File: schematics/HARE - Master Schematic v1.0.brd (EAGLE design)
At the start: 105.1 x 80 mm, 106 parts, among them IC1 NE5532N, IC2 NE5532N, IC3 FT232RL, IC4 NE5532N, IC5 7805DT, IC6 AT25P, J1 9V, J2 STEREOSW, J3 STEREOSW, Q1 16 MHz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

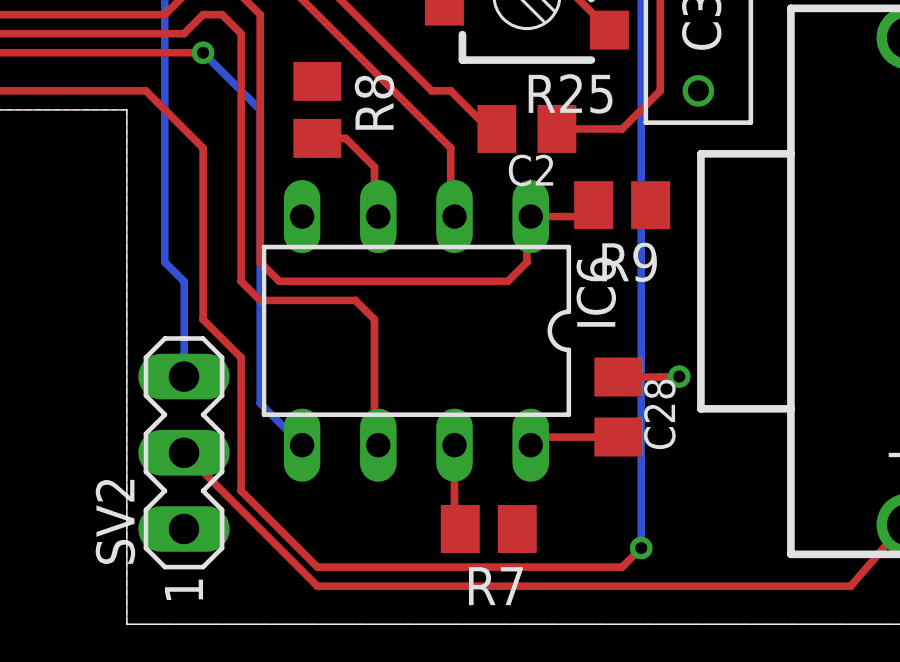
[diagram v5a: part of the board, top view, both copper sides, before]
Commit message: new chip and bootloader
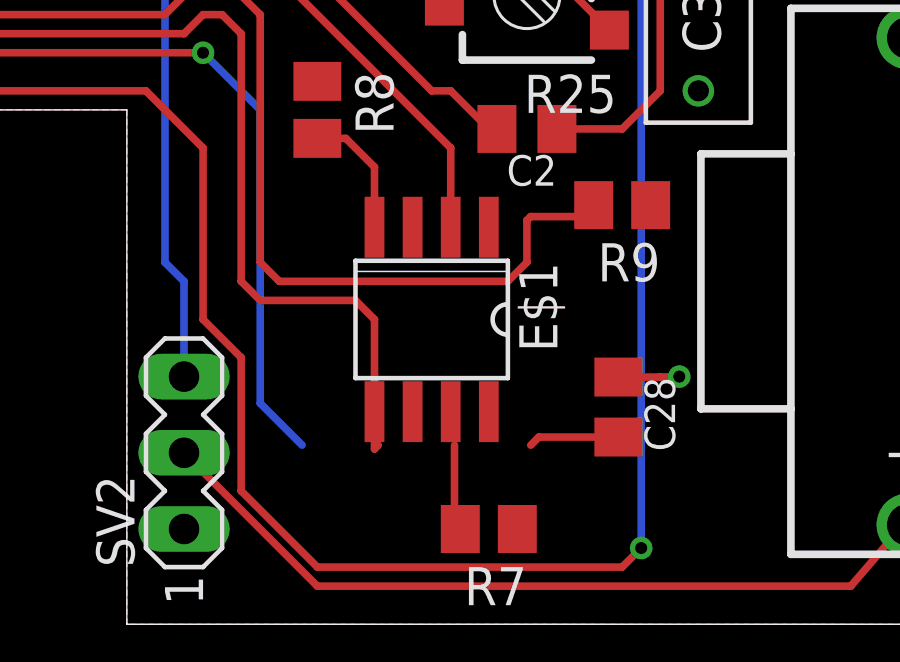
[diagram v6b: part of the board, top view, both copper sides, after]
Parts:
- removed IC6: AT25P, atmel:DIL08
- added E$1: (no value), IS62-65WVS0648:SO08
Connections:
- net +5V: no longer IC6.8
- net GND: no longer IC6.4
- net MEM_CS: no longer IC6.1
- net N$18: no longer IC6.3
- net N$8: no longer IC6.7
- net SPI_MISO: no longer IC6.2
- net SPI_MOSI: no longer IC6.5
- net SPI_SCK: no longer IC6.6
